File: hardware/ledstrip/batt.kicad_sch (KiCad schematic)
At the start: 37 parts, among them J4 BMS connectors, Q10 Q_PMOS, Q5 Q_NMOS, Q6 Q_NMOS, Q7 Q_NMOS, Q8 Q_NMOS, U5 BQ25703A

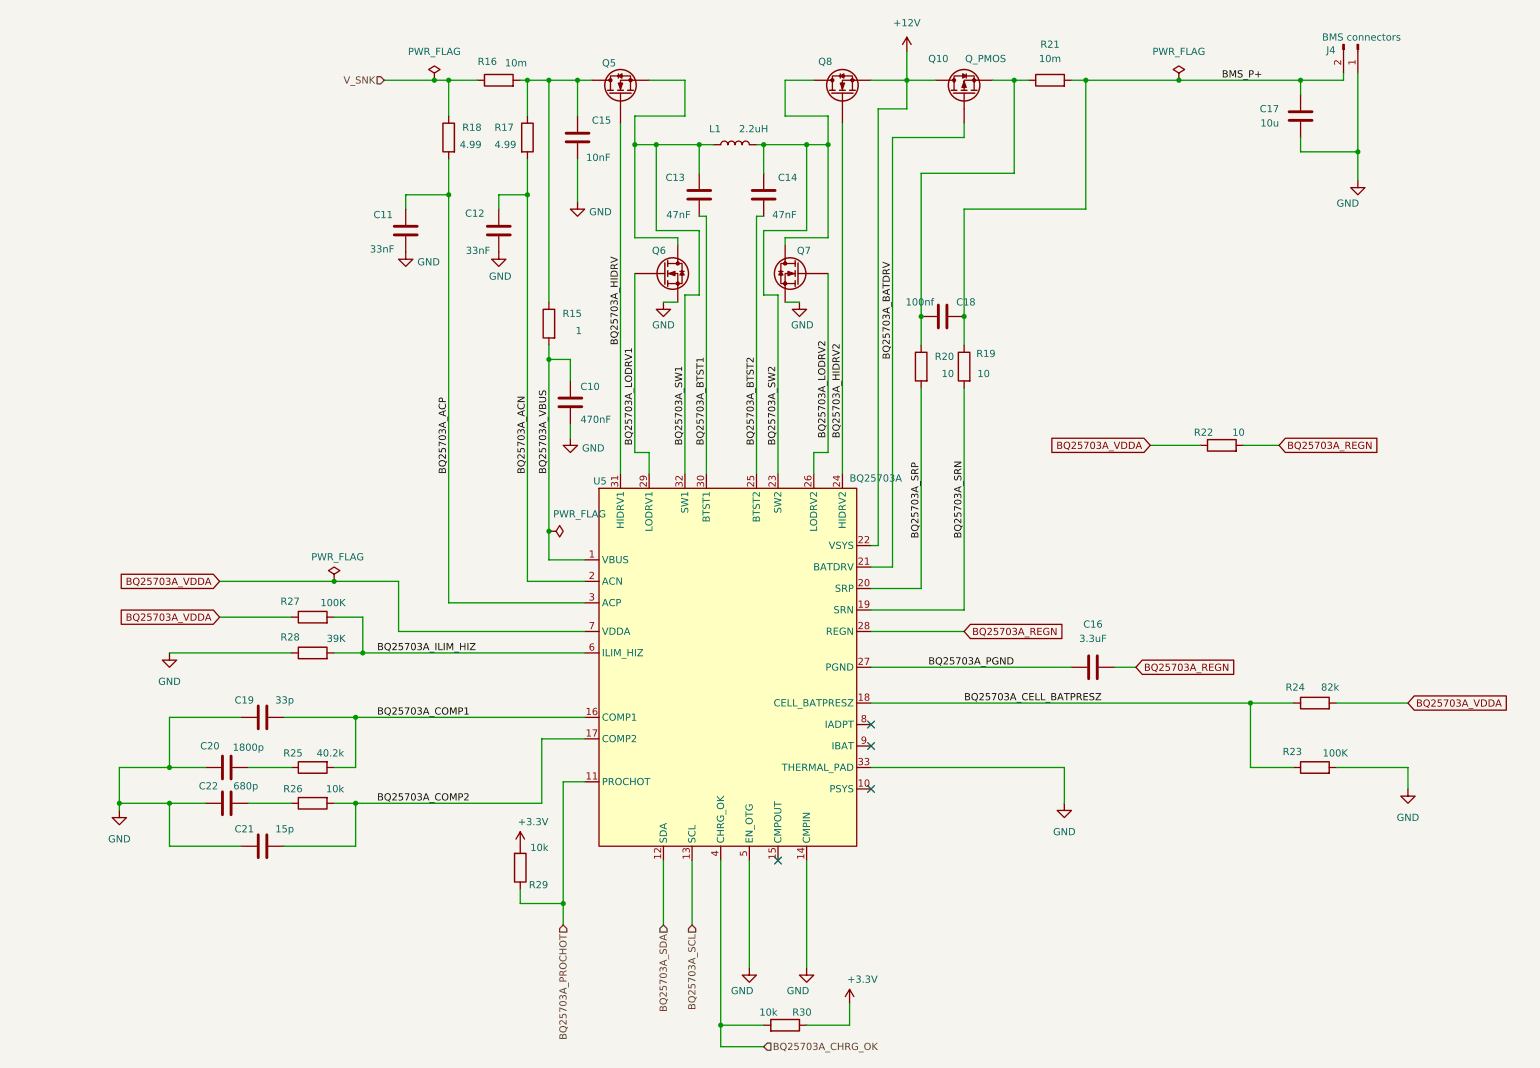
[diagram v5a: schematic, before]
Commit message: Fix ILIM_HIZ setting on BQ25703A
Add comments on schematics about hardware configuration.
Setup a early stable 2.5V from REGN to setup ILIM_HIZ correctly.
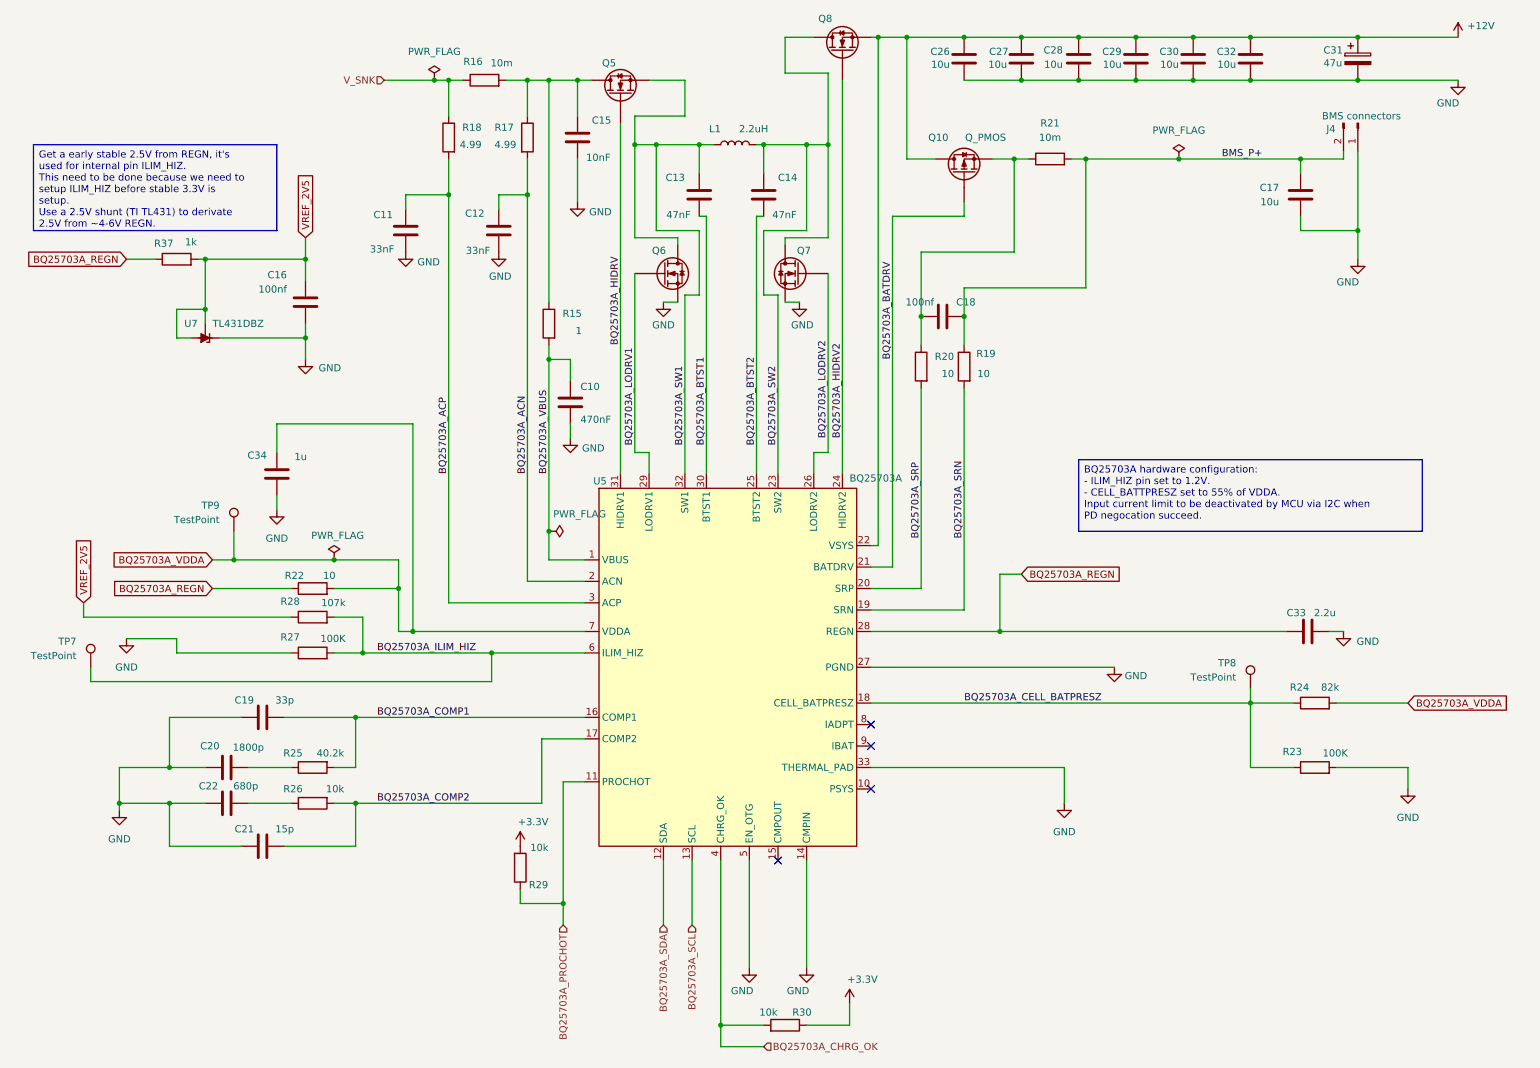
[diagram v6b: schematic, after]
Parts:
- added C26, C27, C28, C29, C30, C32: 10u, Capacitor_SMD:C_0805_2012Metric, symbol Device:C
- added C31: 47u, Capacitor_Tantalum_SMD:CP_EIA-7343-20_Kemet-V, symbol Device:C_Polarized
- added C33: 2.2u, Capacitor_SMD:C_0603_1608Metric, symbol Device:C
- added C34: 1u, Capacitor_SMD:C_0603_1608Metric, symbol Device:C
- added R37: 1k, Capacitor_SMD:C_0603_1608Metric, symbol Device:R
- added TP7, TP8, TP9: TestPoint, TestPoint:TestPoint_Pad_1.0x1.0mm, symbol Connector:TestPoint
- added U7: TL431DBZ, Package_TO_SOT_SMD:SOT-23, symbol Reference_Voltage:TL431DBZ
- C16: value 3.3uF -> 100nf; Distributor Link 1 https://www.mouser.fr/ProductDetail/TDK/C1608X5R1V335K080AC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 -> https://www.mouser.lu/ProductDetail/Samsung-Electro-Mechani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; Distributor Link 2 https://www.digikey.com/en/products/detail/tdk-corporation/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 -> https://www.digikey.com/en/products/detail/samsung-electro-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; Manufacturer (none) -> Samsung; Manufacturer Part Number (none) -> CL10B104KA8VPJC
- R28: value 39K -> 107k; Distributor Link 1 https://www.mouser.fr/ProductDetail/Panasonic/ERA-6ARB393V?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 -> https://www.mouser.fr/ProductDetail/Vishay/CRCW0805107KFKEA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; Distributor Link 2 https://www.digikey.com/en/products/detail/panasonic-electr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 -> https://www.digikey.com/en/products/detail/vishay-dale/CRCW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
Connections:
- net BQ25703A_PGND is gone; now on net GND: C16.2, U5.27 (PGND)
- net +12V: now also C26.1, C27.1, C28.1, C29.1, C30.1, C31.1, C32.1
- net BQ25703A_CELL_BATPRESZ: now also TP8.1
- net BQ25703A_ILIM_HIZ: now also TP7.1
- net BQ25703A_REGN: now also R22.1, C33.1, R37.1; no longer C16.1, R22.2
- net BQ25703A_VDDA: now also R22.2, C34.1, TP9.1; no longer R22.1, R27.1
- net GND: now also R27.1, C26.2, C27.2, C28.2, C29.2, C30.2, C31.2, C32.2, C33.2, C34.2, U7.1 (K); no longer R28.1
- new net VREF_2V5: C16.1, R28.1, R37.2, U7.2 (REF), U7.3 (A)
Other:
- moved on the sheet: C17, J4, Q10, Q8, R16, R21, R22, R27

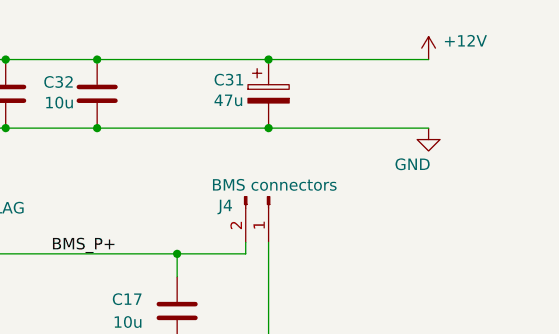
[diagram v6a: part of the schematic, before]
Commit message: Add ON/OFF button to PCB.
Decrease power zone size.
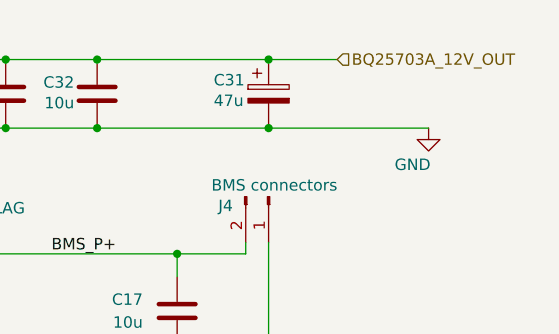
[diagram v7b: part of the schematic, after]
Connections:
- net +12V renamed BQ25703A_12V_OUT
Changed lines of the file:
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@@
 	)
 	(junction
-		(at 111.76 170.18)
+		(at 252.73 16.51)
 		(diameter 0)
 		(color 0 0 0 0)
 	)
 	(junction
-		(at 252.73 16.51)
+		(at 111.76 170.18)
 		(diameter 0)
 		(color 0 0 0 0)
@@
 	(wire
 		(pts
-			(xy 252.73 16.51) (xy 270.51 16.51)
-		)
-		(stroke
-			(width 0)
-			(type default)
-		)
-	)
-	(wire
-		(pts
 			(xy 33.02 152.4) (xy 41.91 152.4)
 		)
@@
 	(wire
 		(pts
+			(xy 252.73 16.51) (xy 260.35 16.51)
+		)
+		(stroke
+			(width 0)
+			(type default)
+		)
+	)
+	(wire
+		(pts
 			(xy 107.95 152.4) (xy 107.95 140.97)
 		)
@@
 		)
 	)
+	(hierarchical_label "BQ25703A_12V_OUT"
+		(shape input)
+		(at 260.35 16.51 0)
+		(effects
+			(font
+				(size 1.27 1.27)
+			)
+			(justify left)
+		)
+	)
 	(hierarchical_label "V_SNK"
 		(shape input)
@@
 					(unit 1)
 				)
-			)
-		)
-	)
-	(symbol
-		(lib_id "power:+12V")
-		(at 270.51 16.51 0)
-		(unit 1)
-		(exclude_from_sim no)
-		(in_bom yes)
-		(on_board yes)
-		(dnp no)
-		(property "Reference" "#PWR037"
-			(at 270.51 20.32 0)
-			(effects
-				(font
-					(size 1.27 1.27)
-				)
-				(hide yes)
-			)
-		)
-		(property "Value" "+12V"
-			(at 274.574 14.478 0)
-			(effects
-				(font
-					(size 1.27 1.27)
-				)
-			)
-		)
-		(property "Footprint" ""
-			(at 270.51 16.51 0)
-			(effects
-				(font
-					(size 1.27 1.27)
-				)
-				(hide yes)
-			)
-		)
-		(property "Datasheet" ""
-			(at 270.51 16.51 0)
-			(effects
-				(font
-					(size 1.27 1.27)
-				)
-				(hide yes)
-			)
-		)
-		(property "Description" "Power symbol creates a global label with name \"+12V\""
-			(at 270.51 16.51 0)
-			(effects
-				(font
-					(size 1.27 1.27)
-				)
-				(hide yes)
-			)
-		)
-		(pin "1"
-		)
-		(instances
-			(project "ledstrip"
-				(path "/dcb997ee-94c4-4df2-ba22-0e091735ddd7/e1352532-a16b-4a34-87fb-bbe36c7f1290"
-					(reference "#PWR037")
-					(unit 1)
-				)
